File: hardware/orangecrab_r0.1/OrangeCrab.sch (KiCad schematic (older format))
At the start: 0 parts

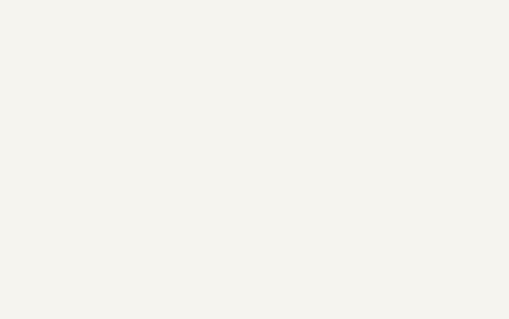
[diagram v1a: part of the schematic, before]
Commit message: Routed more FPGA signals
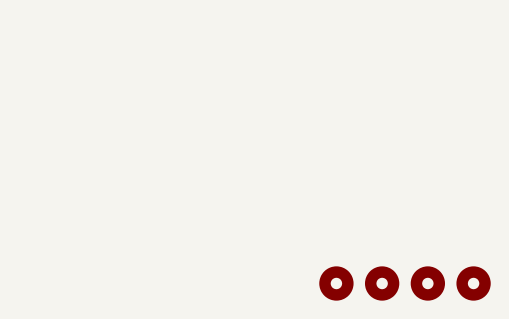
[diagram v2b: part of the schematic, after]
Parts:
- added H1, H2: MountingHole, MountingHole:MountingHole_2.2mm_M2_Pad, symbol Mechanical:MountingHole
- added H3, H4: MountingHole, MountingHole:MountingHole_2.1mm, symbol Mechanical:MountingHole
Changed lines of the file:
@@
 F1 "filePOWER.sch" 60
 $EndSheet
+$Comp
+L Mechanical:MountingHole H4
+U 1 1 5D2429C7
+P 11050 6400
+F 0 "H4" H 11150 6400 50  0001 L CNN
+F 1 "MountingHole" H 11150 6355 50  0001 L CNN
+F 2 "MountingHole:MountingHole_2.1mm" H 11050 6400 50  0001 C CNN
+F 3 "~" H 11050 6400 50  0001 C CNN
+	1    11050 6400
+	1    0    0    -1
+$EndComp
+$Comp
+L Mechanical:MountingHole H3
+U 1 1 5D24316A
+P 10850 6400
+F 0 "H3" H 10950 6400 50  0001 L CNN
+F 1 "MountingHole" H 10950 6355 50  0001 L CNN
+F 2 "MountingHole:MountingHole_2.1mm" H 10850 6400 50  0001 C CNN
+F 3 "~" H 10850 6400 50  0001 C CNN
+	1    10850 6400
+	1    0    0    -1
+$EndComp
+$Comp
+L Mechanical:MountingHole H2
+U 1 1 5D243527
+P 10650 6400
+F 0 "H2" H 10750 6400 50  0001 L CNN
+F 1 "MountingHole" H 10750 6355 50  0001 L CNN
+F 2 "MountingHole:MountingHole_2.2mm_M2_Pad" H 10650 6400 50  0001 C CNN
+F 3 "~" H 10650 6400 50  0001 C CNN
+	1    10650 6400
+	1    0    0    -1
+$EndComp
+$Comp
+L Mechanical:MountingHole H1
+U 1 1 5D243531
+P 10450 6400
+F 0 "H1" H 10550 6400 50  0001 L CNN
+F 1 "MountingHole" H 10550 6355 50  0001 L CNN
+F 2 "MountingHole:MountingHole_2.2mm_M2_Pad" H 10450 6400 50  0001 C CNN
+F 3 "~" H 10450 6400 50  0001 C CNN
+	1    10450 6400
+	1    0    0    -1
+$EndComp
 $EndSCHEMATC

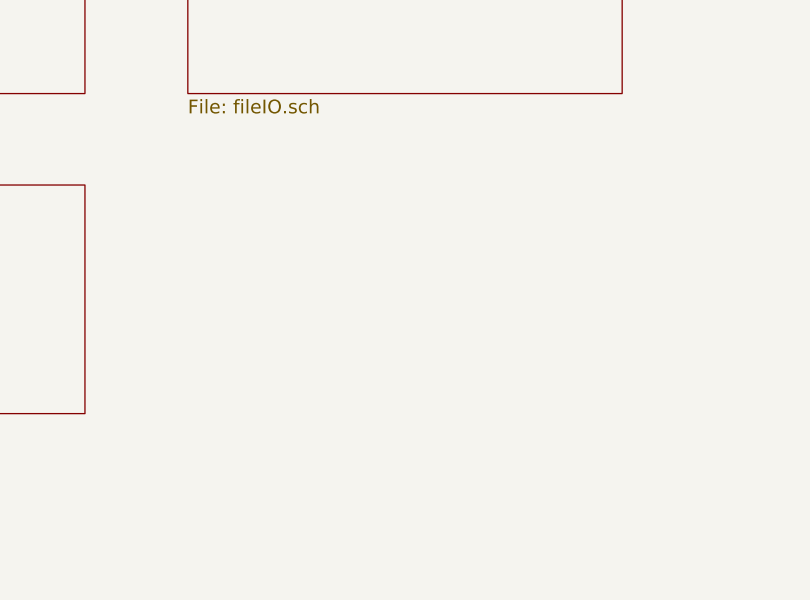
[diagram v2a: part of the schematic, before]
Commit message: Added loads of decoupling capacitors. Added SD card. Started planning out power plane
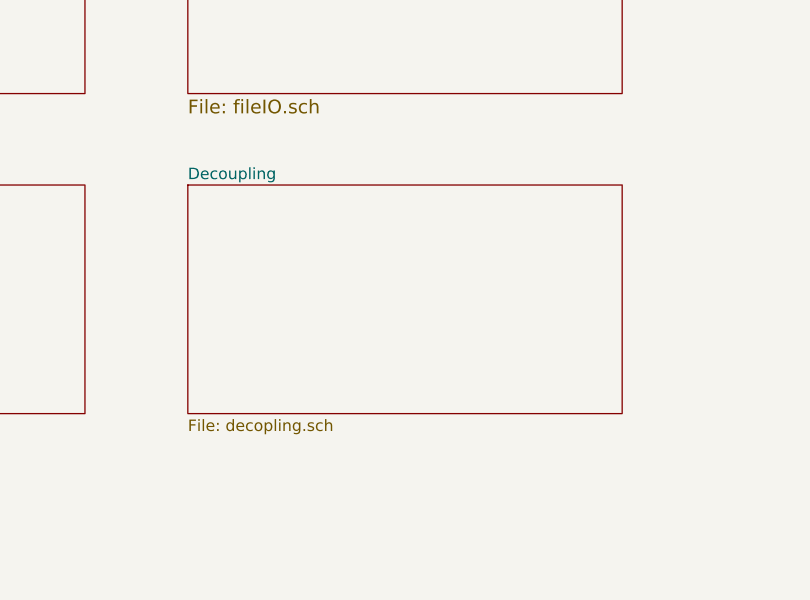
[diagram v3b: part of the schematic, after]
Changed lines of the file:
@@
 $Descr A4 11693 8268
 encoding utf-8
-Sheet 1 6
+Sheet 1 7
 Title "Orange Crab"
 Date "2019-06-28"
@@
 	1    0    0    -1
 $EndComp
+$Sheet
+S 6300 4200 1900 1000
+U 5D35D1F5
+F0 "Decoupling" 50
+F1 "decopling.sch" 50
+$EndSheet
 $EndSCHEMATC
